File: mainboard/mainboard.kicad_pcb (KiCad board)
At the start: 2 copper layers, 110 x 90 mm, 79 parts, among them K1 G6S-2F-5DC, X1 POWER, X10 BUTTONS, X2 IO, X3 INPUT, X4 FRONT INPUT, X5 MAIN OUTPUT, X6 PHONES OUTPUT, X7 UART, X8 DISPLAY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

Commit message: MB fixes
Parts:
- C1, C2, C3, C4: footprint Capacitor_THT:C_Rect_L7.2mm_W4.5mm_P5.00mm_FKS2_FKP2_MKS2_MKP2 -> Capacitor_THT:C_Rect_L7.2mm_W3.5mm_P5.00mm_FKS2_FKP2_MKS2_MKP2
- C6: footprint WAMP:CAPPRD150W45D400H800N -> WAMP:CAPPRD200W45D500H800N
- moved R11 386.8 mm to (112.7, 117.1)
- moved R2 376.6 mm to (172.3, 44.5)
- moved C3 376.1 mm to (101.1, 114.4)
- moved R3 375.7 mm to (180.1, 44.5)
- moved C13 375.7 mm to (143.6, 107.3)
- moved C21 375.7 mm to (143.6, 116.0)
- moved C4 375.7 mm to (101.1, 109.3)
- moved DA3 375.7 mm to (124.7, 102.9)
- moved DA4 375.7 mm to (120.1, 50.4)
- moved DD2 375.7 mm to (173.8, 89.6)
- moved R1 375.7 mm to (176.1, 47.3)
- moved R13 375.7 mm to (141.8, 67.2)
- moved R15 375.7 mm to (182.7, 104.0)
- moved R17 375.7 mm to (177.6, 104.0)
- moved R18 375.7 mm to (175.1, 104.0)
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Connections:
- R11 pad 1: AGND -> Net-(C18-Pad1)
- R11 pad 2: Net-(C18-Pad1) -> AGND
- R12 pad 1: AGND -> Net-(C20-Pad1)
- R12 pad 2: Net-(C20-Pad1) -> AGND
- VT2 pad 1: Net-(R25-Pad2) -> Net-(R25-Pad1)
- VT2 pad 2: Net-(R26-Pad1) -> Net-(R26-Pad2)
- VT3 pad 1: Net-(R26-Pad2) -> Net-(R26-Pad1)
- VT3 pad 2: Net-(R25-Pad1) -> Net-(R25-Pad2)
- X7 pad 1: Net-(R25-Pad1) -> Net-(R25-Pad2)
- X7 pad 2: Net-(R26-Pad1) -> Net-(R26-Pad2)
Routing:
- net Net-(R26-Pad1): track 10.7 -> 3.95 mm
- net Net-(R26-Pad2): track 3.95 -> 10.7 mm
- net /SCL: track 120.1 -> 114.5 mm, vias 7 -> 5
- net Net-(R25-Pad2): track 10.4 -> 14.0 mm
- net Net-(R25-Pad1): track 14.0 -> 10.4 mm
- net AGND: track 19.0 -> 17.2 mm
- net /B_MUTE: track 41.3 -> 40.2 mm
- net Net-(C18-Pad1): track 9.10 -> 10.1 mm
- net /RE_BTN: track 32.7 -> 33.5 mm
- net GND: track 118.9 -> 119.6 mm
- net /B_DEFEAT: track 42.4 -> 43.0 mm
- net /B_PHONES: track 41.3 -> 41.9 mm
- net /B_INPUT: track 40.2 -> 40.7 mm
- net Net-(C3-Pad1): track 7.51 -> 6.98 mm
- net Net-(C2-Pad1): track 7.51 -> 6.98 mm
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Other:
- board text added: "AGND"

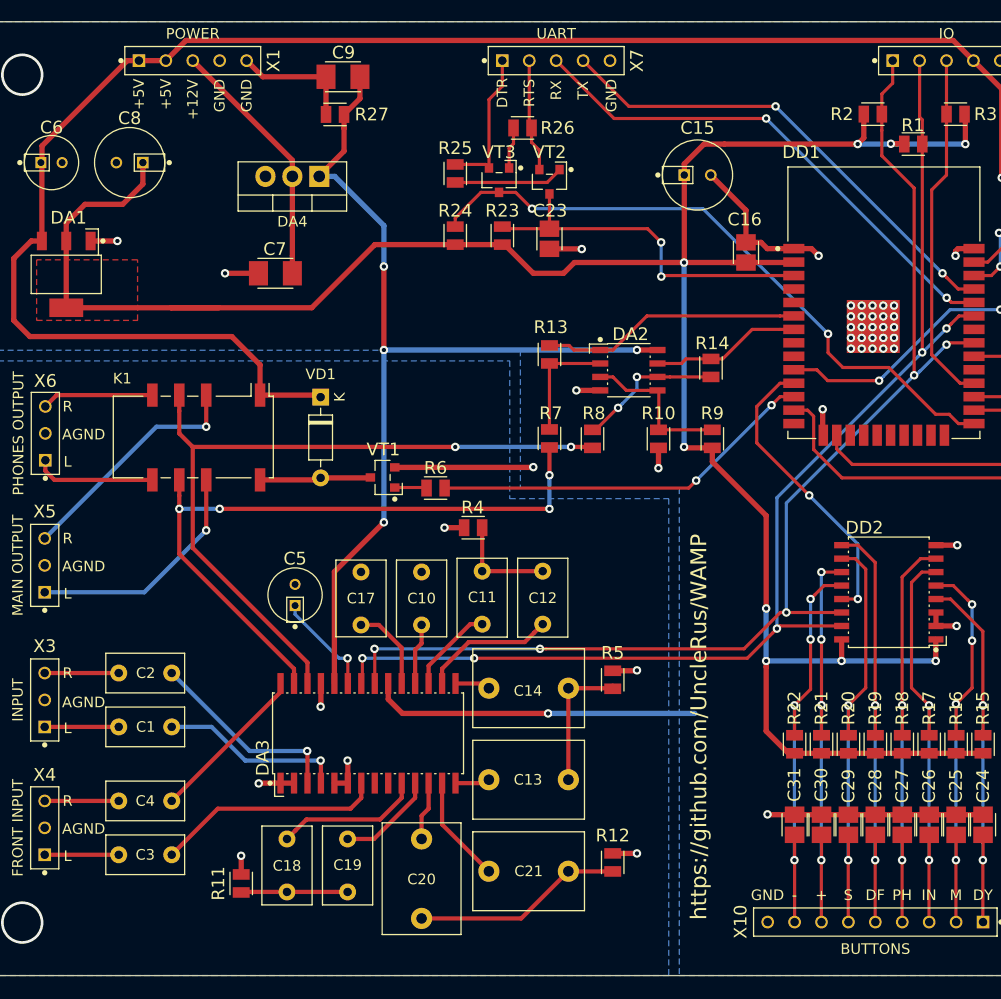
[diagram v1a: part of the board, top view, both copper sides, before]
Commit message: Potentiometers to MB ADC module
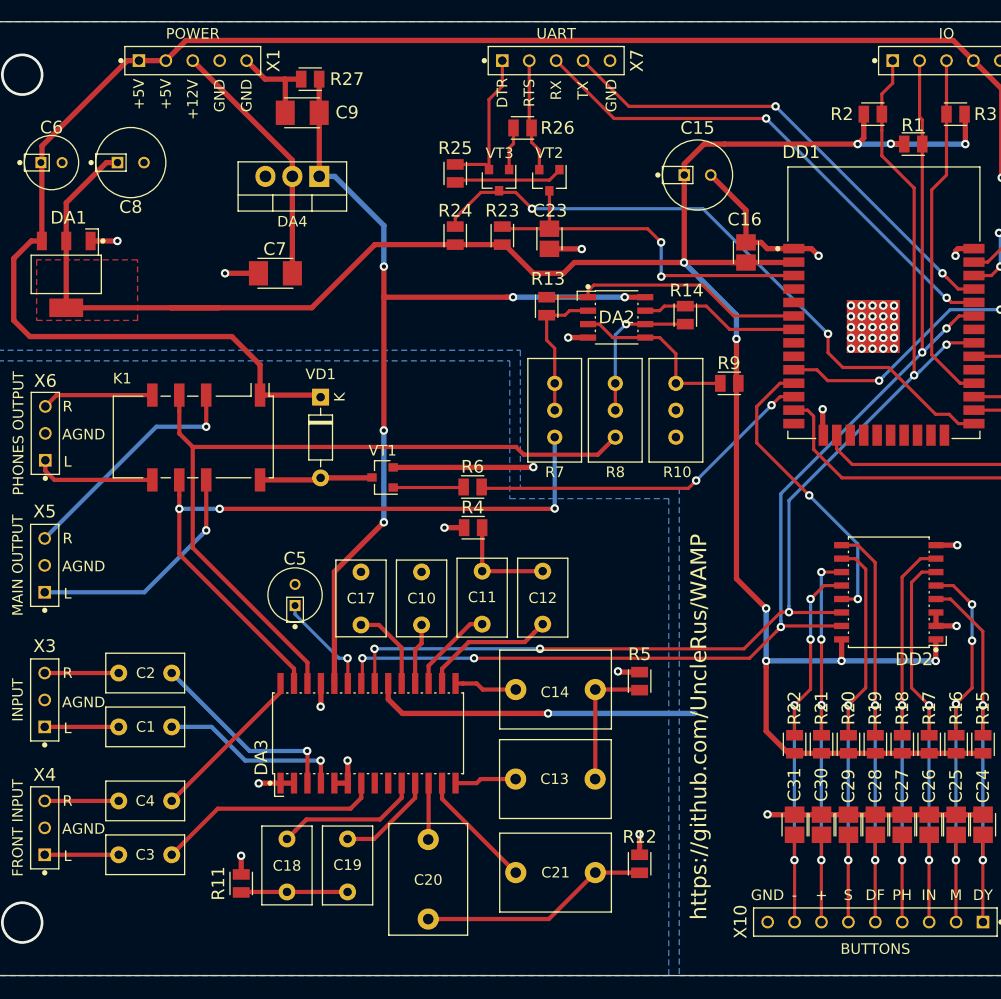
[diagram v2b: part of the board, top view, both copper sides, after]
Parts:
- R10: value 15k -> 50k; footprint WAMP:RESC2013X65N -> Potentiometer_THT:Potentiometer_Bourns_3296W_Vertical
- R13, R14: value 33k -> 50k
- R7, R8: value 150k -> 200k; footprint WAMP:RESC2013X65N -> Potentiometer_THT:Potentiometer_Bourns_3296W_Vertical
- R9: value 100k -> 50k
- VT1, VT2, VT3: footprint WAMP:SOT95P237X112-3N -> Package_TO_SOT_SMD:SOT-23
- moved R14 5.54 mm to (154.6, 63.5)
- moved R10 5.49 mm to (153.7, 69.9), turned to 90 degrees
- moved R9 5.48 mm to (158.7, 69.9), turned to 270 degrees
- moved C9 5.13 mm to (118.5, 44.4)
- moved DA2 5.11 mm to (148.1, 63.7)
- moved R13 4.56 mm to (141.5, 62.6)
- moved R27 4.07 mm to (119.2, 41.2)
- moved R6 3.50 mm to (134.5, 79.7)
- moved C21 2.54 mm to (146.1, 116.1)
- moved C14 2.54 mm to (146.1, 98.8)
- moved R12 2.54 mm to (150.3, 115.3)
- moved R5 2.54 mm to (150.3, 98.0)
- moved C13 2.53 mm to (146.1, 107.3)
- moved R8 2.16 mm to (148.0, 75.0), turned to 270 degrees
- moved C20 0.63 mm to (130.3, 120.5)
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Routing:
- net GND: track 119.6 -> 114.6 mm, vias 38 -> 37
- net +3V3: track 231.5 -> 227.6 mm
- net Net-(R6-Pad1): track 3.02 -> 6.67 mm
- net /PH_SW: track 36.5 -> 33.1 mm
- net /ROUT: track 70.0 -> 73.1 mm, vias 2 -> 0
- net +9V: track 90.0 -> 87.0 mm, vias 4 -> 5
- net /BOUT_L: track 3.33 -> 5.92 mm
- net /BIN_L: track 3.28 -> 5.83 mm
- net Net-(DA2-Pad2): track 11.1 -> 13.4 mm
- net Net-(C20-Pad1): track 19.9 -> 21.8 mm
- net Net-(DA2-Pad3): track 14.7 -> 16.4 mm
- net /LOUT: track 64.4 -> 65.9 mm, vias 4 -> 3
- net /BOUT_R: track 10.1 -> 11.3 mm
- net /ADC7: track 14.1 -> 15.1 mm
- net /ADC6: track 24.6 -> 25.3 mm
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
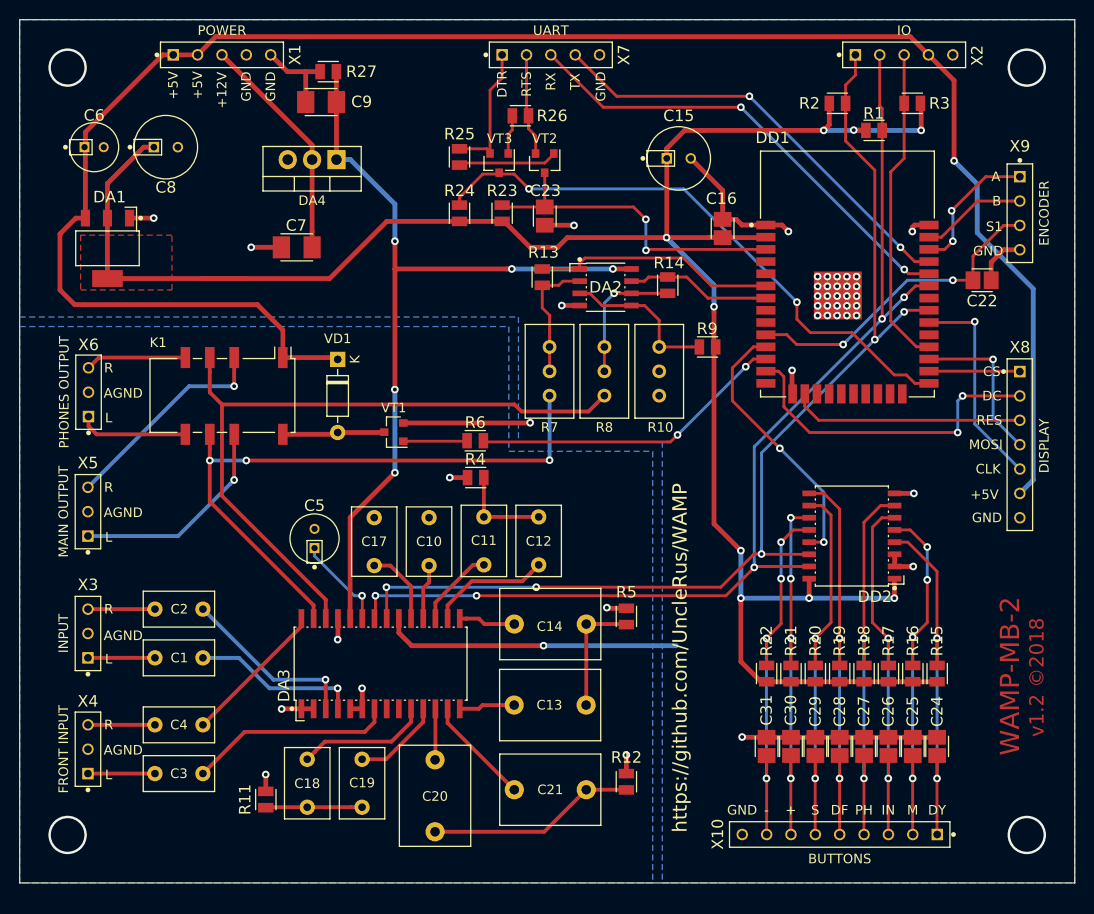
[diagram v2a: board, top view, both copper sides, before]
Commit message: Added blocking caps to ADC input
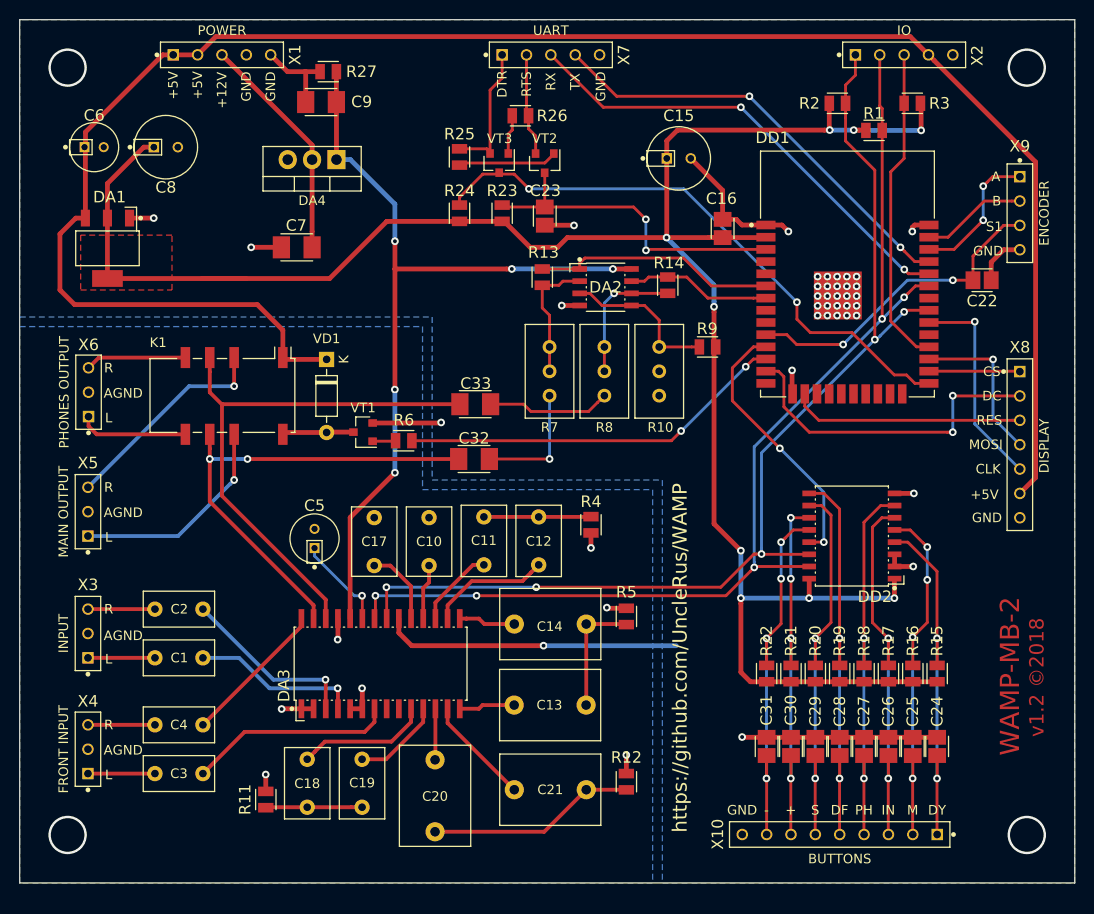
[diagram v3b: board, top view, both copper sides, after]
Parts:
- added C32: 1uF, WAMP:CAPC3216X180N, F.Cu at (134.4, 81.6)
- added C33: 1uF, WAMP:CAPC3216X180N, F.Cu at (134.5, 75.9)
- R9: value 50k -> 100k
- moved R4 13.0 mm to (146.6, 88.5), turned to 180 degrees
- moved R6 7.45 mm to (127.1, 79.7)
- moved VT1 3.20 mm to (122.8, 78.8)
- moved VD1 1.16 mm to (119.0, 71.2)
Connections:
- R7 pad 1: /LOUT -> Net-(C32-Pad2)
- R8 pad 1: /ROUT -> Net-(C33-Pad2)
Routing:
- net /LOUT: track 65.9 -> 49.6 mm, vias 3 -> 2
- net /ROUT: track 73.1 -> 57.0 mm
- net Net-(C32-Pad2): track 0.00 -> 12.9 mm, vias 0 -> 1
- net Net-(C33-Pad2): track 0.00 -> 12.9 mm
- net /PH_SW: track 33.1 -> 40.4 mm
- net GND: track 114.6 -> 108.6 mm
- net Net-(R6-Pad1): track 6.67 -> 2.42 mm
- net Net-(K1-Pad10): track 10.5 -> 7.45 mm
- net Net-(C11-Pad1): track 9.82 -> 11.2 mm
- net +5V: track 195.4 -> 194.5 mm, vias 1 -> 0
- net +3V3: track 227.6 -> 228.4 mm

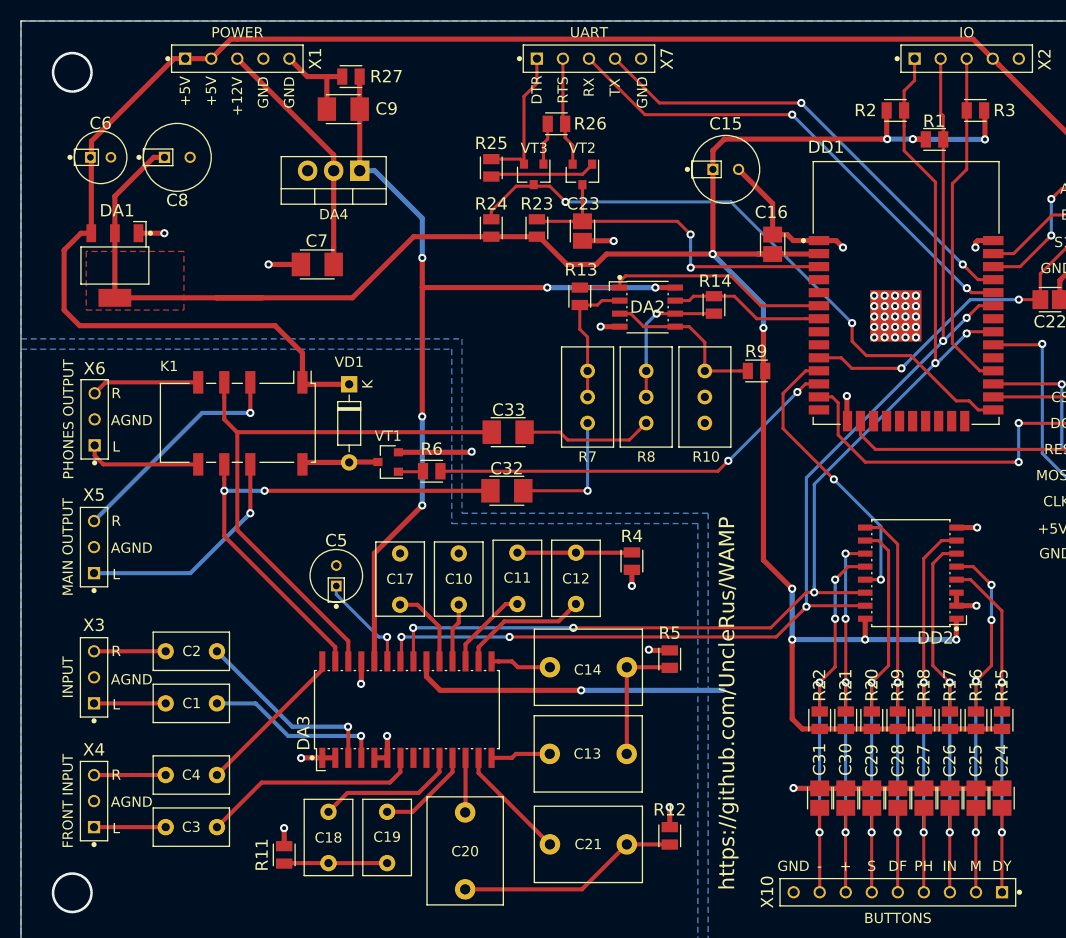
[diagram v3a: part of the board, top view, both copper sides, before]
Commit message: MB 7809 pinout fixed
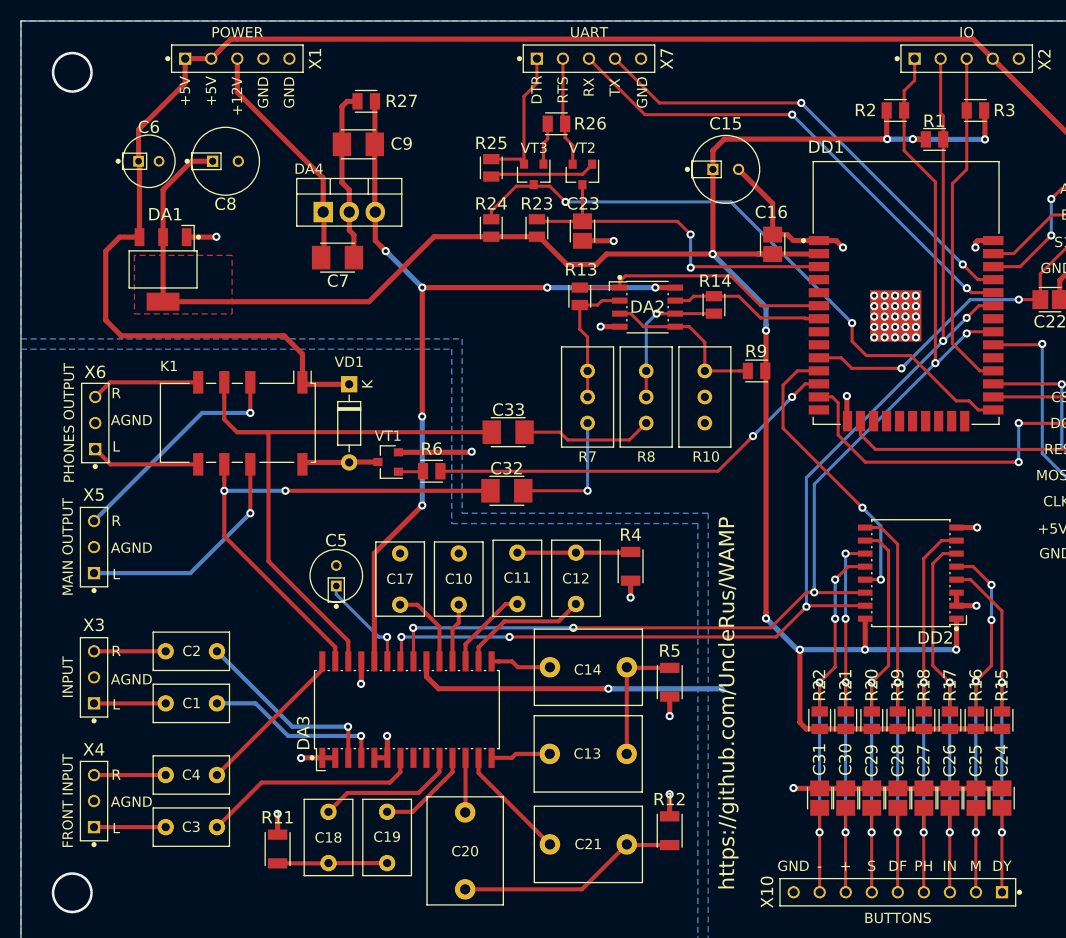
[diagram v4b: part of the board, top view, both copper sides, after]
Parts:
- DA4: value L7809 -> L7809P
- R11, R12, R4, R5: footprint WAMP:RESC2013X65N -> WAMP:RESC3115X65N
- moved DA4 5.38 mm to (116.5, 54.4), turned to 0 degrees
- moved C6 4.71 mm to (99.5, 49.5)
- moved C8 4.71 mm to (107.0, 49.5)
- moved DA1 4.71 mm to (100.9, 60.0)
- moved C9 3.73 mm to (119.9, 47.8)
- moved R27 2.83 mm to (120.7, 43.6)
- moved R5 2.25 mm to (150.3, 100.3), turned to 180 degrees
- moved C7 2.08 mm to (117.9, 58.9), turned to 90 degrees
- moved R11 0.86 mm to (112.1, 116.5)
- moved R4 0.52 mm to (146.5, 89.0)
- moved R12 0.50 mm to (150.3, 114.8)
- moved X6 0.36 mm to (94.3, 75.0)
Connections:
- DA4 pad 1: +9V -> Net-(C7-Pad1)
- DA4 pad 2: Net-(C7-Pad1) -> GND
- DA4 pad 3: GND -> +9V
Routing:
- net +3V3: track 228.4 -> 221.1 mm
- net +5V: track 194.5 -> 189.2 mm
- net GND: track 108.6 -> 113.8 mm, vias 37 -> 36
- net +9V: track 87.0 -> 83.1 mm, vias 5 -> 6
- net /ROUT: track 57.0 -> 58.7 mm
- net Net-(C7-Pad1): track 24.0 -> 22.5 mm
- net Net-(K1-Pad6): track 11.5 -> 10.7 mm
- net Net-(C18-Pad1): track 10.1 -> 10.7 mm
